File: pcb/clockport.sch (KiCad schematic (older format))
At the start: 1 part

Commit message: Some work done on the whole project
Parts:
- gave numbers to parts that had none: 1
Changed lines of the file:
@@
 $EndDescr
 $Comp
-L WM1200:clockport_connector X?
+L WM1200:clockport_connector X2
 U 1 1 5E55E9B8
 P 3250 2900
-F 0 "X?" H 3250 3600 50  0000 C CNN
+F 0 "X2" H 3250 3600 50  0000 C CNN
 F 1 "clockport_connector" H 3250 2850 50  0000 C CNN
 F 2 "" H 3250 3550 50  0001 C CNN
@@
 Text Label 4500 2800 0    50   ~ 0
 A5
-Text HLabel 1000 1000 0    50   BiDi ~ 0
-TRPDR
 Text HLabel 1000 3000 0    50   Input ~ 0
 POWER_GND
@@
 Wire Bus Line
 	5000 1000 5000 4000
+Text HLabel 1000 1000 0    50   BiDi ~ 0
+TRPDR
 $EndSCHEMATC

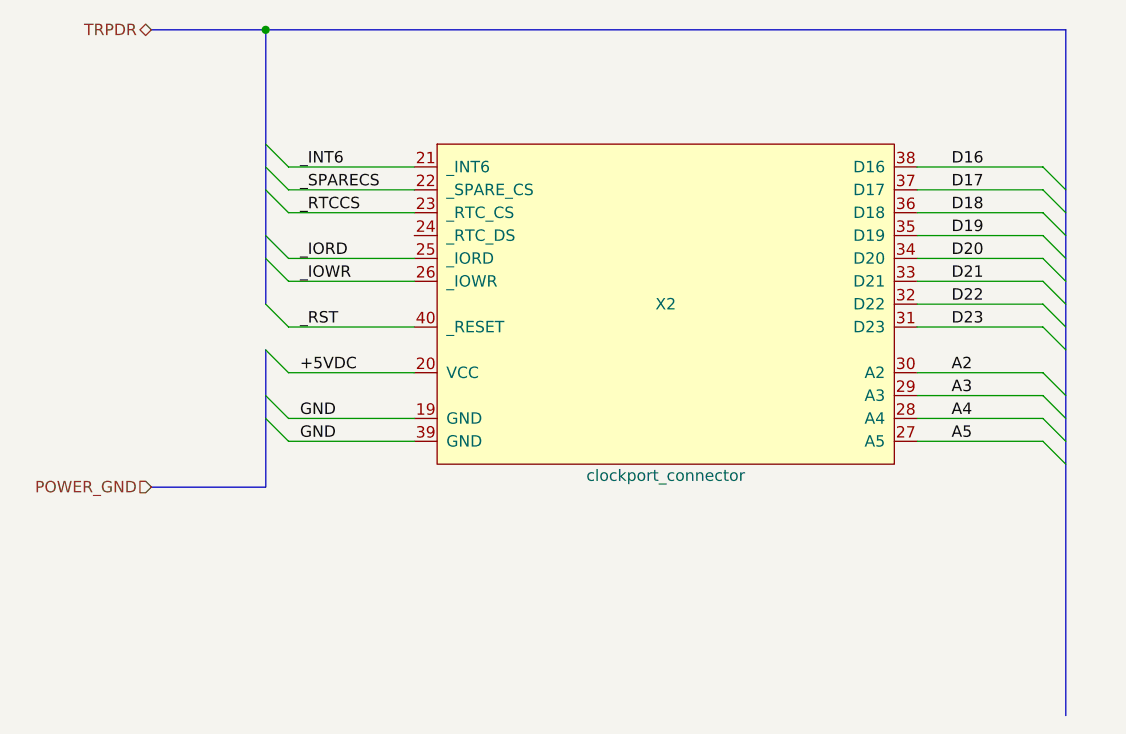
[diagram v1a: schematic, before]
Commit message: The scheme needs it's buses to be remade because of the way KiCad works, ok
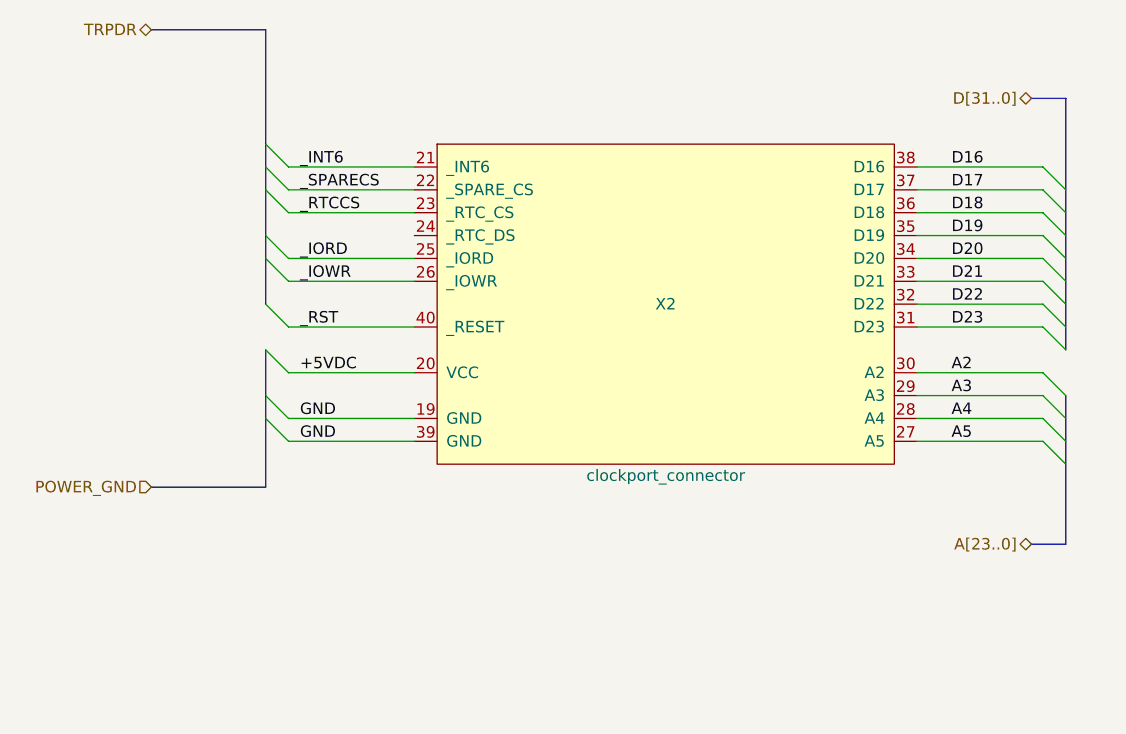
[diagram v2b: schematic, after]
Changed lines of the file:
@@
 $Descr A4 11693 8268
 encoding utf-8
-Sheet 3 11
+Sheet 11 11
 Title "WishMaster 1200"
 Date ""
@@
 Wire Bus Line
 	1000 1000 1500 1000
-Connection ~ 1500 1000
-Wire Bus Line
-	1500 1000 5000 1000
 Wire Bus Line
 	1500 3000 1000 3000
+Text HLabel 1000 1000 0    50   BiDi ~ 0
+TRPDR
+Wire Bus Line
+	5000 3250 4850 3250
+Wire Bus Line
+	4850 1300 5000 1300
 Wire Bus Line
 	1500 2400 1500 3000
 Wire Bus Line
+	5000 2600 5000 3250
+Wire Bus Line
 	1500 1000 1500 2200
 Wire Bus Line
-	5000 1000 5000 4000
-Text HLabel 1000 1000 0    50   BiDi ~ 0
-TRPDR
+	5000 1300 5000 2400
+Text HLabel 4850 1300 0    50   BiDi ~ 0
+D[31..0]
+Text HLabel 4850 3250 0    50   BiDi ~ 0
+A[23..0]
 $EndSCHEMATC

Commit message: ok, we are using global labels now
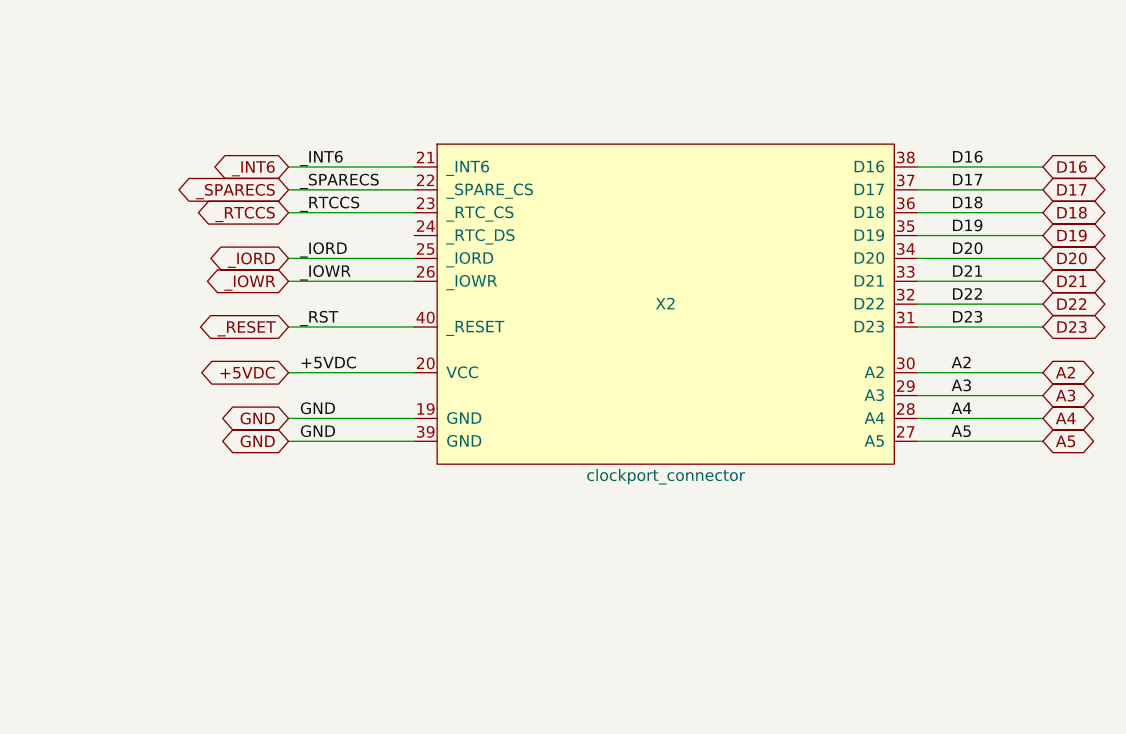
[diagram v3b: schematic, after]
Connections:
- net _RST renamed _RESET
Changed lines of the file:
@@
 $Descr A4 11693 8268
 encoding utf-8
-Sheet 11 11
+Sheet 10 11
 Title "WishMaster 1200"
 Date ""
@@
 	1    0    0    -1
 $EndComp
-Entry Wire Line
-	1500 1500 1600 1600
-Entry Wire Line
-	1500 1600 1600 1700
-Entry Wire Line
-	1500 1700 1600 1800
-Entry Wire Line
-	1500 1900 1600 2000
-Entry Wire Line
-	1500 2000 1600 2100
-Entry Wire Line
-	1500 2200 1600 2300
-Entry Wire Line
-	1500 2400 1600 2500
-Entry Wire Line
-	1500 2600 1600 2700
-Entry Wire Line
-	1500 2700 1600 2800
-Entry Wire Line
-	4900 1600 5000 1700
-Entry Wire Line
-	4900 1700 5000 1800
-Entry Wire Line
-	4900 1800 5000 1900
-Entry Wire Line
-	4900 1900 5000 2000
-Entry Wire Line
-	4900 2000 5000 2100
-Entry Wire Line
-	4900 2100 5000 2200
-Entry Wire Line
-	4900 2200 5000 2300
-Entry Wire Line
-	4900 2300 5000 2400
-Entry Wire Line
-	4900 2500 5000 2600
-Entry Wire Line
-	4900 2600 5000 2700
-Entry Wire Line
-	4900 2700 5000 2800
-Entry Wire Line
-	4900 2800 5000 2900
 Wire Wire Line
 	2150 1600 1600 1600
@@
 Text Label 4500 2800 0    50   ~ 0
 A5
-Text HLabel 1000 3000 0    50   Input ~ 0
-POWER_GND
-Wire Bus Line
-	1000 1000 1500 1000
-Wire Bus Line
-	1500 3000 1000 3000
-Text HLabel 1000 1000 0    50   BiDi ~ 0
-TRPDR
-Wire Bus Line
-	5000 3250 4850 3250
-Wire Bus Line
-	4850 1300 5000 1300
-Wire Bus Line
-	1500 2400 1500 3000
-Wire Bus Line
-	5000 2600 5000 3250
-Wire Bus Line
-	1500 1000 1500 2200
-Wire Bus Line
-	5000 1300 5000 2400
-Text HLabel 4850 1300 0    50   BiDi ~ 0
-D[31..0]
-Text HLabel 4850 3250 0    50   BiDi ~ 0
-A[23..0]
+Text GLabel 1600 1600 0    50   BiDi ~ 0
+_INT6
+Text GLabel 1600 1700 0    50   BiDi ~ 0
+_SPARECS
+Text GLabel 1600 1800 0    50   BiDi ~ 0
+_RTCCS
+Text GLabel 1600 2000 0    50   BiDi ~ 0
+_IORD
+Text GLabel 1600 2100 0    50   BiDi ~ 0
+_IOWR
+Text GLabel 1600 2300 0    50   BiDi ~ 0
+_RESET
+Text GLabel 1600 2500 0    50   BiDi ~ 0
++5VDC
+Text GLabel 1600 2700 0    50   BiDi ~ 0
+GND
+Text GLabel 1600 2800 0    50   BiDi ~ 0
+GND
+Text GLabel 4900 1600 2    50   BiDi ~ 0
+D16
+Text GLabel 4900 1700 2    50   BiDi ~ 0
+D17
+Text GLabel 4900 1800 2    50   BiDi ~ 0
+D18
+Text GLabel 4900 1900 2    50   BiDi ~ 0
+D19
+Text GLabel 4900 2000 2    50   BiDi ~ 0
+D20
+Text GLabel 4900 2100 2    50   BiDi ~ 0
+D21
+Text GLabel 4900 2200 2    50   BiDi ~ 0
+D22
+Text GLabel 4900 2300 2    50   BiDi ~ 0
+D23
+Text GLabel 4900 2500 2    50   BiDi ~ 0
+A2
+Text GLabel 4900 2600 2    50   BiDi ~ 0
+A3
+Text GLabel 4900 2700 2    50   BiDi ~ 0
+A4
+Text GLabel 4900 2800 2    50   BiDi ~ 0
+A5
 $EndSCHEMATC

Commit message: fpga-side gpio connector added
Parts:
- renumbered X2 to X4
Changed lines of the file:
@@
 $Descr A4 11693 8268
 encoding utf-8
-Sheet 10 11
+Sheet 9 11
 Title "WishMaster 1200"
 Date ""
@@
 $EndDescr
 $Comp
-L WM1200:clockport_connector X2
+L WM1200:clockport_connector X4
 U 1 1 5E55E9B8
 P 3250 2900
-F 0 "X2" H 3250 3600 50  0000 C CNN
+F 0 "X4" H 3250 3600 50  0000 C CNN
 F 1 "clockport_connector" H 3250 2850 50  0000 C CNN
 F 2 "" H 3250 3550 50  0001 C CNN

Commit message: more footprints assigned
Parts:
- renumbered X4 to X3
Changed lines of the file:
@@
 $EndDescr
 $Comp
-L WM1200:clockport_connector X4
+L WM1200:clockport_connector X3
 U 1 1 5E55E9B8
 P 3250 2900
-F 0 "X4" H 3250 3600 50  0000 C CNN
+F 0 "X3" H 3250 3600 50  0000 C CNN
 F 1 "clockport_connector" H 3250 2850 50  0000 C CNN
 F 2 "" H 3250 3550 50  0001 C CNN

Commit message: More footprints assigned
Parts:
- X3: footprint (none) -> WM1200:clockport
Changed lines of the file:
@@
 F 0 "X3" H 3250 3600 50  0000 C CNN
 F 1 "clockport_connector" H 3250 2850 50  0000 C CNN
-F 2 "" H 3250 3550 50  0001 C CNN
+F 2 "WM1200:clockport" H 3250 3550 50  0001 C CNN
 F 3 "" H 3250 3550 50  0001 C CNN
 	1    3250 2900
